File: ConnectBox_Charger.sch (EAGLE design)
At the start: 12 parts, among them IC1 M24C32-RDW6TP, J1 CONNECTOR_PI_40_PIN, J2 Lithium Cell, J3 microUSB Power In, J4 FTDI Serial, J5 5V Charger Output, U1 LTC4040

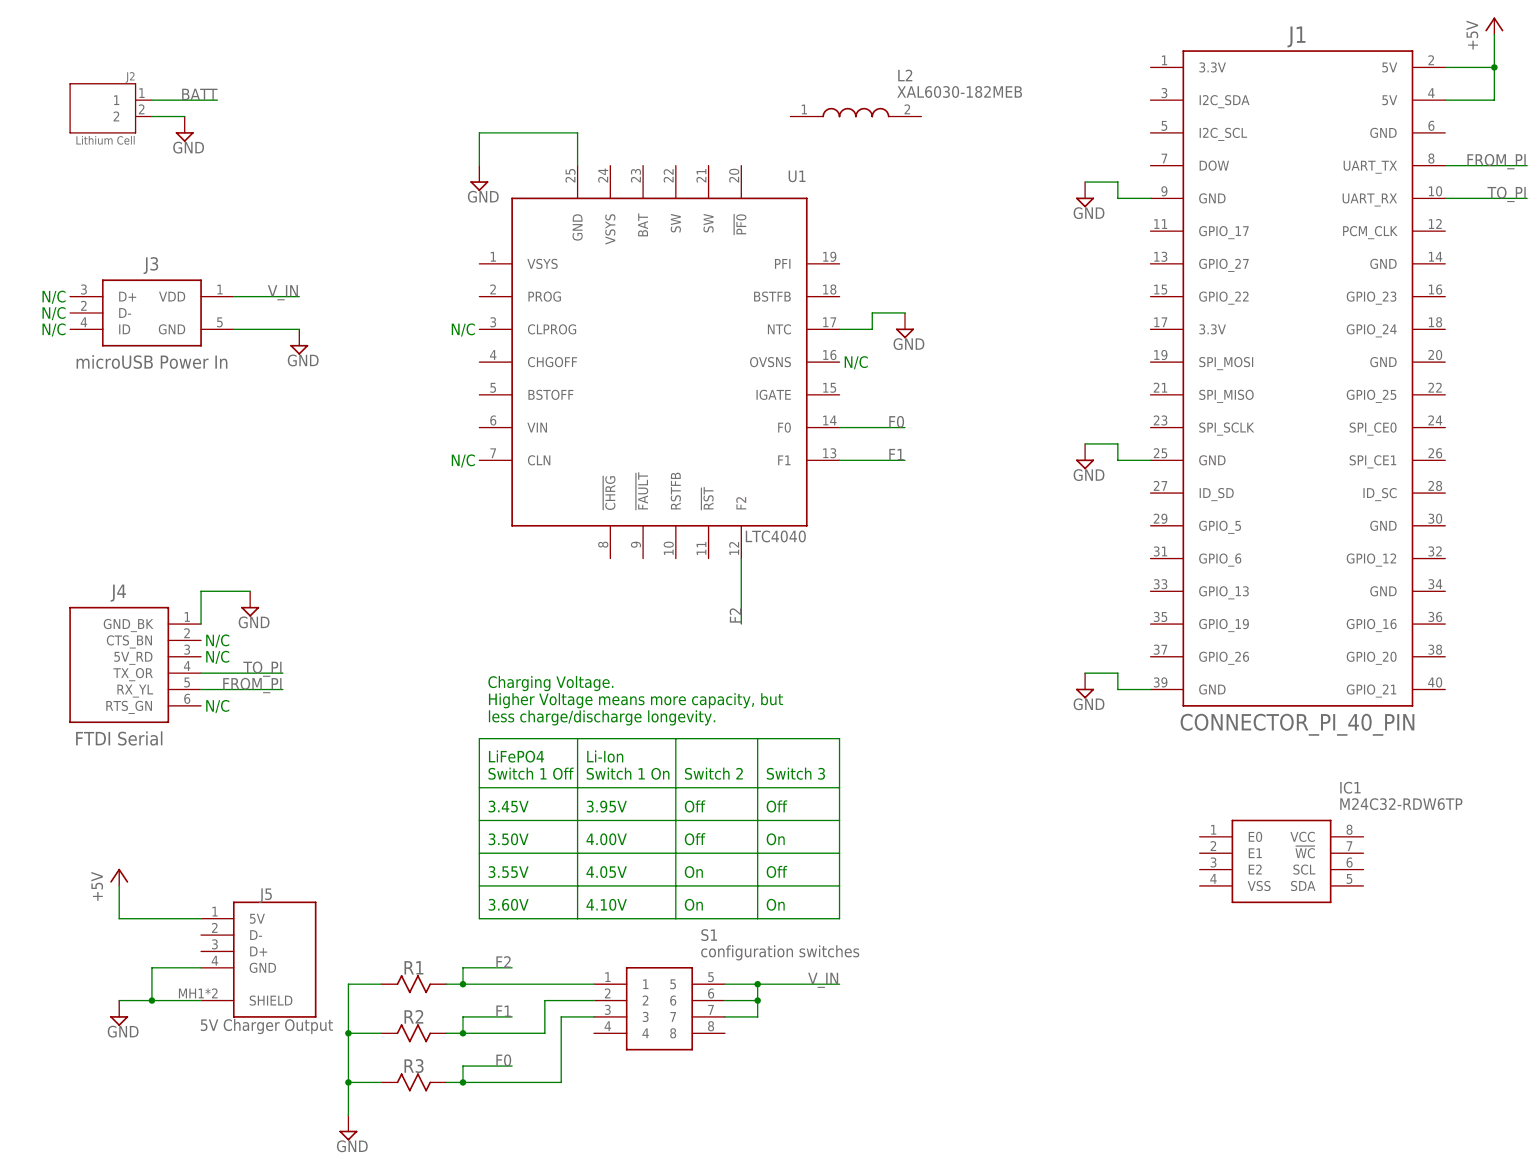
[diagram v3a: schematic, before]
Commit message: Update LTC4040 and Pi 40-pin connector to 0.1" pin spacing versions to save space on schematic.
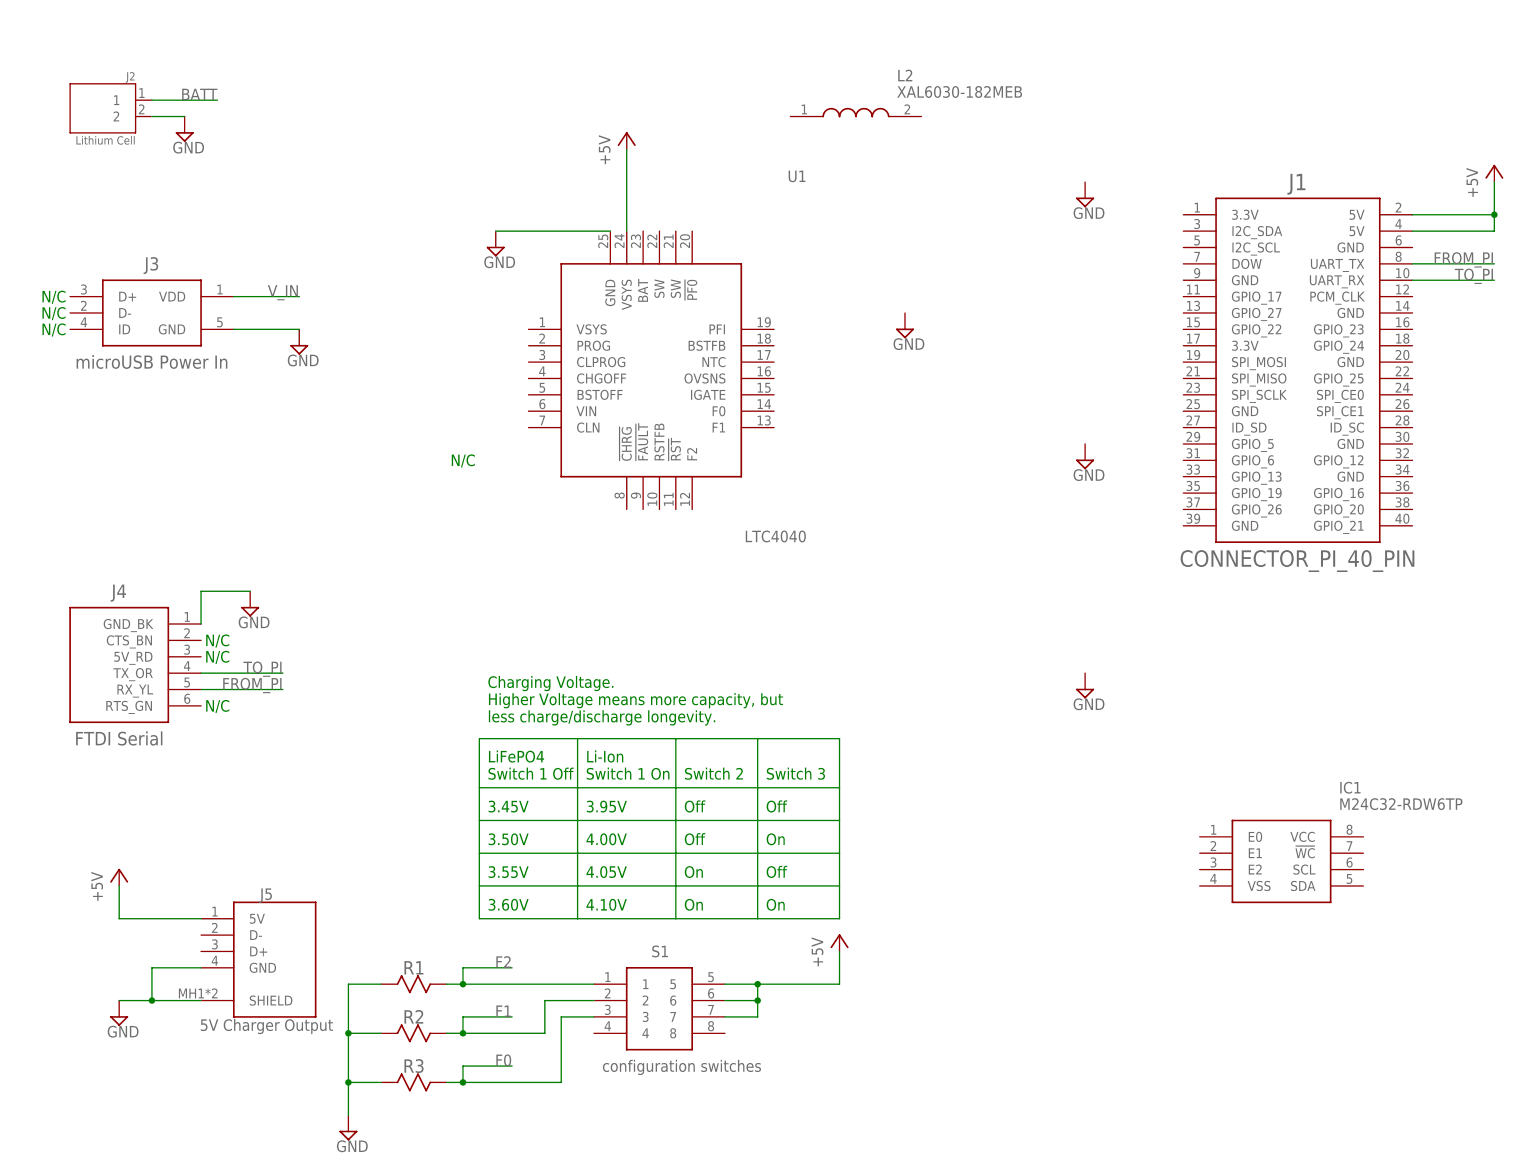
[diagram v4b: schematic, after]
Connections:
- net +5V: now also S1.5, S1.6, S1.7, U1.VSYS@24
- net F0: no longer U1.F0@14
- net F1: no longer U1.F1@13
- net F2: no longer U1.F2@12
- net GND: no longer J1.GND@25, J1.GND@39, J1.GND@9, U1.NTC@17
- net V_IN: no longer S1.5, S1.6, S1.7
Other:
- note added: "Todo: Resistors at USB-A to indicate output current 100uF low ESR for LTC4040 Vsys"
- note removed: "Todo: Resistors at USB-A to indicate output current"
- moved on the sheet: J1, U1

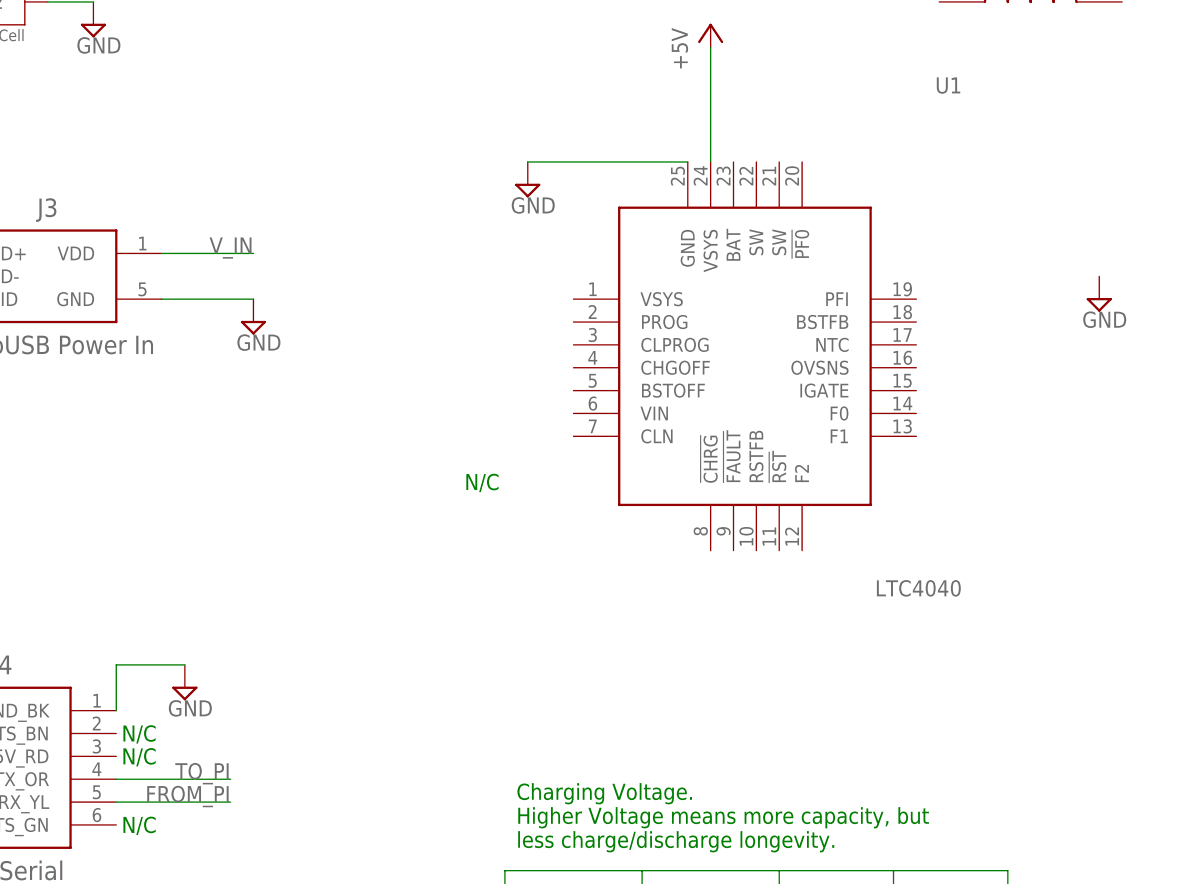
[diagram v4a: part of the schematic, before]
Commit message: Start connecting LTC4040 charge control IC.
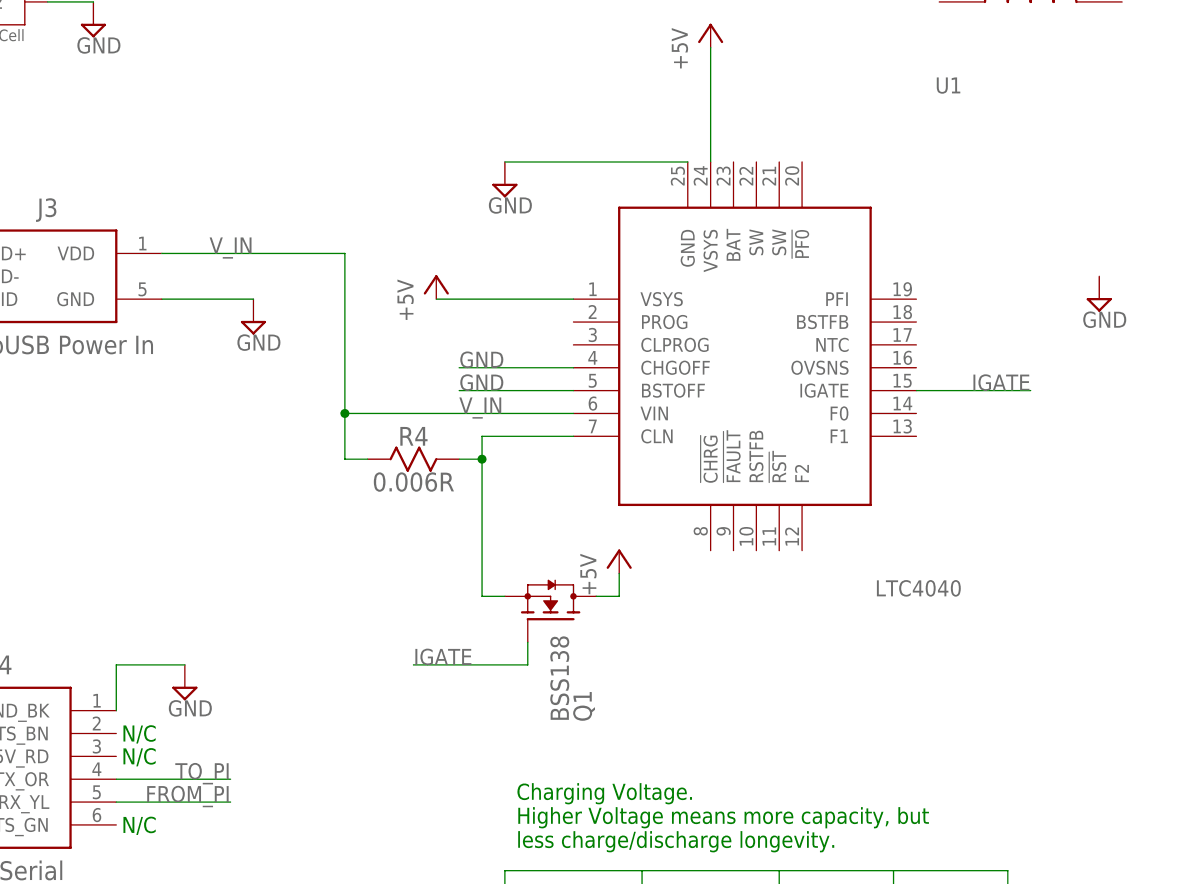
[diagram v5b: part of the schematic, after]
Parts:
- added Q1: BSS138, APU_ENGR480_UPS_EAGLE_Library:BSS138
- added R4: 0.006R, ConnectBox_2019:RESISTOR0603
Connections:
- new net IGATE: Q1.G, U1.IGATE@15
- new net N$2: Q1.S, R4.2, U1.CLN@7
- net +5V: now also Q1.D, U1.VSYS@1
- net GND: now also U1.BSTOFF@5, U1.CHGOFF@4
- net V_IN: now also R4.1, U1.VIN@6
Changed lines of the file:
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@@
 <part name="J4" library="ConnectBox_2019" deviceset="CONNECTOR-6-FTDI" device="" value="FTDI Serial"/>
 <part name="SUPPLY1" library="ConnectBox_2019" deviceset="GND" device=""/>
-<part name="SUPPLY2" library="ConnectBox_2019" deviceset="GND" device=""/>
 <part name="SUPPLY3" library="ConnectBox_2019" deviceset="GND" device=""/>
 <part name="SUPPLY4" library="ConnectBox_2019" deviceset="GND" device=""/>
@@
 <part name="P+3" library="ConnectBox_2019" deviceset="+5V" device=""/>
 <part name="P+4" library="ConnectBox_2019" deviceset="+5V" device=""/>
+<part name="SUPPLY2" library="ConnectBox_2019" deviceset="GND" device=""/>
+<part name="R4" library="ConnectBox_2019" deviceset="RESISTOR" device="0603" value="0.006R"/>
+<part name="Q1" library="APU_ENGR480_UPS_EAGLE_Library" deviceset="BSS138" device=""/>
+<part name="P+5" library="ConnectBox_2019" deviceset="+5V" device=""/>
+<part name="P+6" library="ConnectBox_2019" deviceset="+5V" device=""/>
 </parts>
 <sheets>
@@
 <text x="33.02" y="81.28" size="1.778" layer="91" align="center">N/C</text>
 <text x="33.02" y="73.66" size="1.778" layer="91" align="center">N/C</text>
-<text x="71.12" y="111.76" size="1.778" layer="91" align="center">N/C</text>
 <text x="90.17" y="62.23" size="1.778" layer="91">Li-Ion
 Switch 1 On</text>
@@
 <attribute name="VALUE" x="26.035" y="159.385" size="1.778" layer="96"/>
 </instance>
-<instance part="SUPPLY2" gate="GND" x="76.2" y="144.78" smashed="yes">
-<attribute name="VALUE" x="74.295" y="141.605" size="1.778" layer="96"/>
-</instance>
 <instance part="SUPPLY3" gate="GND" x="167.64" y="76.2" smashed="yes">
 <attribute name="VALUE" x="165.735" y="73.025" size="1.778" layer="96"/>
@@
 <instance part="P+4" gate="1" x="129.54" y="38.1" smashed="yes">
 <attribute name="VALUE" x="127" y="33.02" size="1.778" layer="96" rot="R90"/>
+</instance>
+<instance part="SUPPLY2" gate="GND" x="73.66" y="144.78" smashed="yes">
+<attribute name="VALUE" x="71.755" y="141.605" size="1.778" layer="96"/>
+</instance>
+<instance part="R4" gate="G$1" x="63.5" y="114.3" smashed="yes">
+<attribute name="VALUE" x="63.5" y="111.76" size="2.0828" layer="96" align="center"/>
+<attribute name="NAME" x="63.5" y="116.84" size="2.0828" layer="95" align="center"/>
+</instance>
+<instance part="Q1" gate="G$1" x="78.74" y="96.52" smashed="yes" rot="MR90">
+<attribute name="VALUE" x="78.74" y="85.09" size="2.032" layer="96" rot="MR90"/>
+<attribute name="NAME" x="81.28" y="85.09" size="2.032" layer="95" rot="MR90"/>
+</instance>
+<instance part="P+5" gate="1" x="86.36" y="104.14" smashed="yes">
+<attribute name="VALUE" x="83.82" y="99.06" size="1.778" layer="96" rot="R90"/>
+</instance>
+<instance part="P+6" gate="1" x="66.04" y="134.62" smashed="yes">
+<attribute name="VALUE" x="63.5" y="129.54" size="1.778" layer="96" rot="R90"/>
 </instance>
 </instances>
@@
 <segment>
 <pinref part="U1" gate="G$1" pin="GND@25"/>
+<wire x1="73.66" y1="147.32" x2="93.98" y2="147.32" width="0.1524" layer="91"/>
 <pinref part="SUPPLY2" gate="GND" pin="GND"/>
-<wire x1="76.2" y1="147.32" x2="93.98" y2="147.32" width="0.1524" layer="91"/>
+</segment>
+<segment>
+<pinref part="U1" gate="G$1" pin="BSTOFF@5"/>
+<wire x1="81.28" y1="121.92" x2="68.58" y2="121.92" width="0.1524" layer="91"/>
+<label x="68.58" y="121.92" size="1.778" layer="95"/>
+</segment>
+<segment>
+<pinref part="U1" gate="G$1" pin="CHGOFF@4"/>
+<wire x1="81.28" y1="124.46" x2="68.58" y2="124.46" width="0.1524" layer="91"/>
+<label x="68.58" y="124.46" size="1.778" layer="95"/>
 </segment>
 </net>
@@
 <segment>
 <pinref part="J3" gate="G$1" pin="VDD"/>
-<wire x1="45.72" y1="137.16" x2="35.56" y2="137.16" width="0.1524" layer="91"/>
 <label x="45.72" y="137.16" size="1.778" layer="95" rot="MR0"/>
+<wire x1="35.56" y1="137.16" x2="55.88" y2="137.16" width="0.1524" layer="91"/>
+<wire x1="55.88" y1="137.16" x2="55.88" y2="119.38" width="0.1524" layer="91"/>
+<pinref part="U1" gate="G$1" pin="VIN@6"/>
+<label x="68.58" y="119.38" size="1.778" layer="95"/>
+<wire x1="55.88" y1="119.38" x2="81.28" y2="119.38" width="0.1524" layer="91"/>
+<wire x1="55.88" y1="119.38" x2="55.88" y2="114.3" width="0.1524" layer="91"/>
+<junction x="55.88" y="119.38"/>
+<pinref part="R4" gate="G$1" pin="1"/>
+<wire x1="55.88" y1="114.3" x2="58.42" y2="114.3" width="0.1524" layer="91"/>
 </segment>
 </net>
@@
 <junction x="116.84" y="27.94"/>
 <pinref part="P+4" gate="1" pin="+5V"/>
+</segment>
+<segment>
+<pinref part="Q1" gate="G$1" pin="D"/>
+<pinref part="P+5" gate="1" pin="+5V"/>
+<wire x1="86.36" y1="101.6" x2="86.36" y2="99.06" width="0.1524" layer="91"/>
+<wire x1="86.36" y1="99.06" x2="83.82" y2="99.06" width="0.1524" layer="91"/>
+</segment>
+<segment>
+<pinref part="U1" gate="G$1" pin="VSYS@1"/>
+<pinref part="P+6" gate="1" pin="+5V"/>
+<wire x1="66.04" y1="132.08" x2="81.28" y2="132.08" width="0.1524" layer="91"/>
 </segment>
 </net>
@@
 </segment>
 </net>
+<net name="N$2" class="0">
+<segment>
+<pinref part="R4" gate="G$1" pin="2"/>
+<wire x1="68.58" y1="114.3" x2="71.12" y2="114.3" width="0.1524" layer="91"/>
+<wire x1="71.12" y1="114.3" x2="71.12" y2="116.84" width="0.1524" layer="91"/>
+<pinref part="U1" gate="G$1" pin="CLN@7"/>
+<wire x1="71.12" y1="116.84" x2="81.28" y2="116.84" width="0.1524" layer="91"/>
+<wire x1="71.12" y1="114.3" x2="71.12" y2="99.06" width="0.1524" layer="91"/>
+<junction x="71.12" y="114.3"/>
+<pinref part="Q1" gate="G$1" pin="S"/>
+<wire x1="71.12" y1="99.06" x2="73.66" y2="99.06" width="0.1524" layer="91"/>
+</segment>
+</net>
+<net name="IGATE" class="0">
+<segment>
+<pinref part="U1" gate="G$1" pin="IGATE@15"/>
+<wire x1="132.08" y1="121.92" x2="119.38" y2="121.92" width="0.1524" layer="91"/>
+<label x="132.08" y="121.92" size="1.778" layer="95" rot="MR0"/>
+</segment>
+<segment>
+<wire x1="63.5" y1="91.44" x2="76.2" y2="91.44" width="0.1524" layer="91"/>
+<pinref part="Q1" gate="G$1" pin="G"/>
+<wire x1="76.2" y1="91.44" x2="76.2" y2="93.98" width="0.1524" layer="91"/>
+<label x="63.5" y="91.44" size="1.778" layer="95"/>
+</segment>
+</net>
